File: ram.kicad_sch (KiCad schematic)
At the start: 44 parts, among them IC2 MT41K256M16TW-107_P

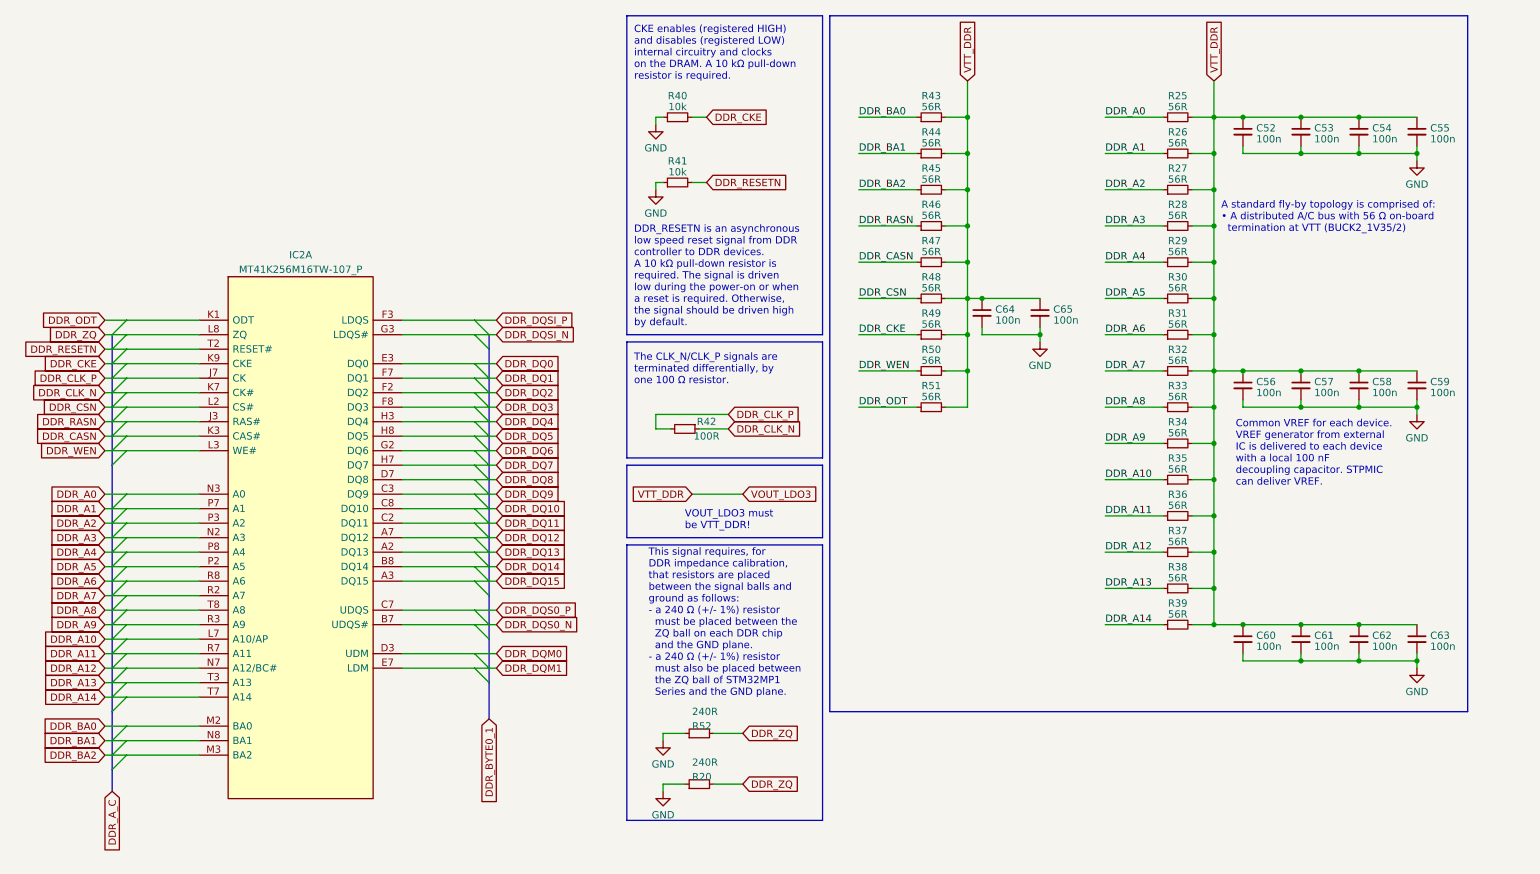
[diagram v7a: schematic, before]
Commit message: added QSMP1570 symbol and footprint to project. Modified Symbol. Cleaning of schematic.
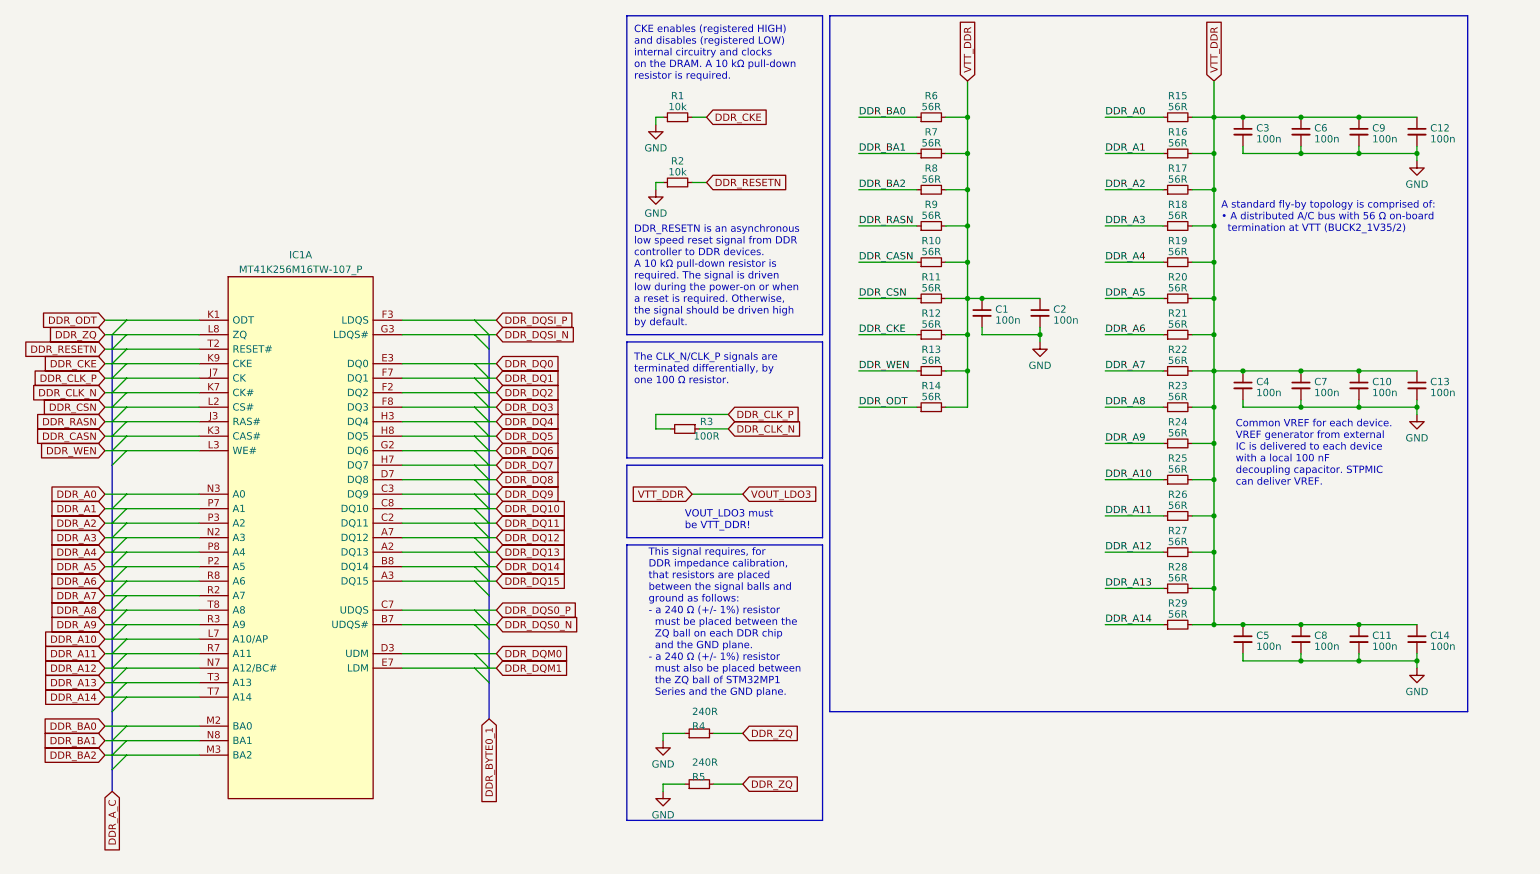
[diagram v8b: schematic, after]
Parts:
- renumbered C64 to C1, C58 to C10, C62 to C11, C55 to C12, C59 to C13, C63 to C14, C65 to C2, C52 to C3, C56 to C4, C60 to C5, C53 to C6, C57 to C7, C61 to C8, C54 to C9, IC2 to IC1, R40 to R1, R47 to R10, R48 to R11, R49 to R12, R50 to R13, R51 to R14, R25 to R15, R26 to R16, R27 to R17, R28 to R18, R29 to R19, R41 to R2, R30 to R20, R31 to R21, R32 to R22, R33 to R23, R34 to R24, R35 to R25, R36 to R26, R37 to R27, R38 to R28, R39 to R29, R42 to R3, R52 to R4, R20 to R5, R43 to R6, R44 to R7, R45 to R8, R46 to R9
